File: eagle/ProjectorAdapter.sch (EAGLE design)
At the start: 8 parts, among them J1 0532610271, J3 0532610471, J4 0532610271

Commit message: updated pcb with molex connectors; created 6 pin connector. updated code for different pin definitions.
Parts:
- removed J4: 0532610271, volks73-Molex:0532610271
- added J2: 05339805711, volks73-Molex:05339805711
- J1: value 0532610271 -> 05339805711; device volks73-Molex:0532610271 -> volks73-Molex:05339805711
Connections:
- net FROM_PROJ: now also J2-2.P$1; no longer J4-1.P$1
- net GND: now also J1-3.P$1, J2-3.P$1; no longer J1-1.P$1, J4-2.P$1
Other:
- moved on the sheet: J1-1, J1-2
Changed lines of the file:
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@@
 <part name="GND3" library="SparkFun-Aesthetics" deviceset="GND" device=""/>
 <part name="J3" library="volks73-Molex" deviceset="0532610471" device=""/>
-<part name="J1" library="volks73-Molex" deviceset="0532610271" device=""/>
-<part name="J4" library="volks73-Molex" deviceset="0532610271" device=""/>
+<part name="J1" library="volks73-Molex" deviceset="05339805711" device=""/>
+<part name="J2" library="volks73-Molex" deviceset="05339805711" device=""/>
 <part name="GND1" library="SparkFun-Aesthetics" deviceset="GND" device=""/>
 <part name="GND4" library="SparkFun-Aesthetics" deviceset="GND" device=""/>
@@
 <instance part="J3" gate="-3" x="93.98" y="-27.94"/>
 <instance part="J3" gate="-4" x="93.98" y="-38.1"/>
-<instance part="J1" gate="-1" x="127" y="25.4"/>
-<instance part="J1" gate="-2" x="127" y="30.48"/>
-<instance part="J4" gate="-1" x="-15.24" y="33.02" rot="R180"/>
-<instance part="J4" gate="-2" x="-15.24" y="25.4" rot="R180"/>
-<instance part="GND1" gate="1" x="-7.62" y="7.62"/>
-<instance part="GND4" gate="1" x="114.3" y="5.08"/>
+<instance part="J1" gate="-1" x="139.7" y="40.64"/>
+<instance part="J1" gate="-2" x="139.7" y="27.94"/>
+<instance part="J1" gate="-3" x="139.7" y="17.78"/>
+<instance part="J1" gate="-4" x="139.7" y="7.62"/>
+<instance part="J1" gate="-5" x="142.24" y="-7.62"/>
+<instance part="J1" gate="-6" x="139.7" y="-20.32"/>
+<instance part="J2" gate="-1" x="-30.48" y="58.42" rot="R180"/>
+<instance part="J2" gate="-2" x="-30.48" y="45.72" rot="R180"/>
+<instance part="J2" gate="-3" x="-30.48" y="33.02" rot="R180"/>
+<instance part="J2" gate="-4" x="-30.48" y="25.4" rot="R180"/>
+<instance part="J2" gate="-5" x="-30.48" y="15.24" rot="R180"/>
+<instance part="J2" gate="-6" x="-30.48" y="-5.08" rot="R180"/>
+<instance part="GND1" gate="1" x="0" y="20.32"/>
+<instance part="GND4" gate="1" x="111.76" y="10.16"/>
 </instances>
 <busses>
@@
 </segment>
 <segment>
-<pinref part="J4" gate="-2" pin="P$1"/>
-<wire x1="-10.16" y1="25.4" x2="-7.62" y2="25.4" width="0.1524" layer="91"/>
-<wire x1="-7.62" y1="25.4" x2="-7.62" y2="10.16" width="0.1524" layer="91"/>
+<pinref part="J2" gate="-3" pin="P$1"/>
+<wire x1="-25.4" y1="33.02" x2="-2.54" y2="33.02" width="0.1524" layer="91"/>
 <pinref part="GND1" gate="1" pin="GND"/>
+<wire x1="-2.54" y1="33.02" x2="0" y2="33.02" width="0.1524" layer="91"/>
+<wire x1="0" y1="33.02" x2="0" y2="22.86" width="0.1524" layer="91"/>
 </segment>
 <segment>
-<wire x1="114.3" y1="25.4" x2="114.3" y2="7.62" width="0.1524" layer="91"/>
+<pinref part="J1" gate="-3" pin="P$1"/>
+<wire x1="134.62" y1="17.78" x2="111.76" y2="17.78" width="0.1524" layer="91"/>
+<wire x1="111.76" y1="17.78" x2="111.76" y2="12.7" width="0.1524" layer="91"/>
 <pinref part="GND4" gate="1" pin="GND"/>
-<pinref part="J1" gate="-1" pin="P$1"/>
-<wire x1="121.92" y1="25.4" x2="114.3" y2="25.4" width="0.1524" layer="91"/>
 </segment>
 </net>
@@
 <net name="FROM_PROJ" class="0">
 <segment>
-<pinref part="J4" gate="-1" pin="P$1"/>
-<wire x1="-10.16" y1="33.02" x2="-2.54" y2="33.02" width="0.1524" layer="91"/>
-<label x="0" y="33.02" size="1.778" layer="95"/>
-</segment>
-<segment>
 <pinref part="TEENSY_LEFT" gate="G$1" pin="4"/>
 <wire x1="40.64" y1="45.72" x2="30.48" y2="45.72" width="0.1524" layer="91"/>
 <label x="22.86" y="45.72" size="1.778" layer="95"/>
+</segment>
+<segment>
+<pinref part="J2" gate="-2" pin="P$1"/>
+<wire x1="-25.4" y1="45.72" x2="0" y2="45.72" width="0.1524" layer="91"/>
+<label x="-5.08" y="48.26" size="1.778" layer="95"/>
 </segment>
 </net>
@@
 </segment>
 </net>
-<net name="N$1" class="0">
+<net name="N$4" class="0">
 <segment>
+<pinref part="J1" gate="-2" pin="P$1"/>
+<wire x1="121.92" y1="27.94" x2="134.62" y2="27.94" width="0.1524" layer="91"/>
 <pinref part="R1" gate="G$1" pin="2"/>
-<pinref part="J1" gate="-2" pin="P$1"/>
 <wire x1="114.3" y1="30.48" x2="121.92" y2="30.48" width="0.1524" layer="91"/>
+<wire x1="121.92" y1="27.94" x2="121.92" y2="30.48" width="0.1524" layer="91"/>
 </segment>
 </net>

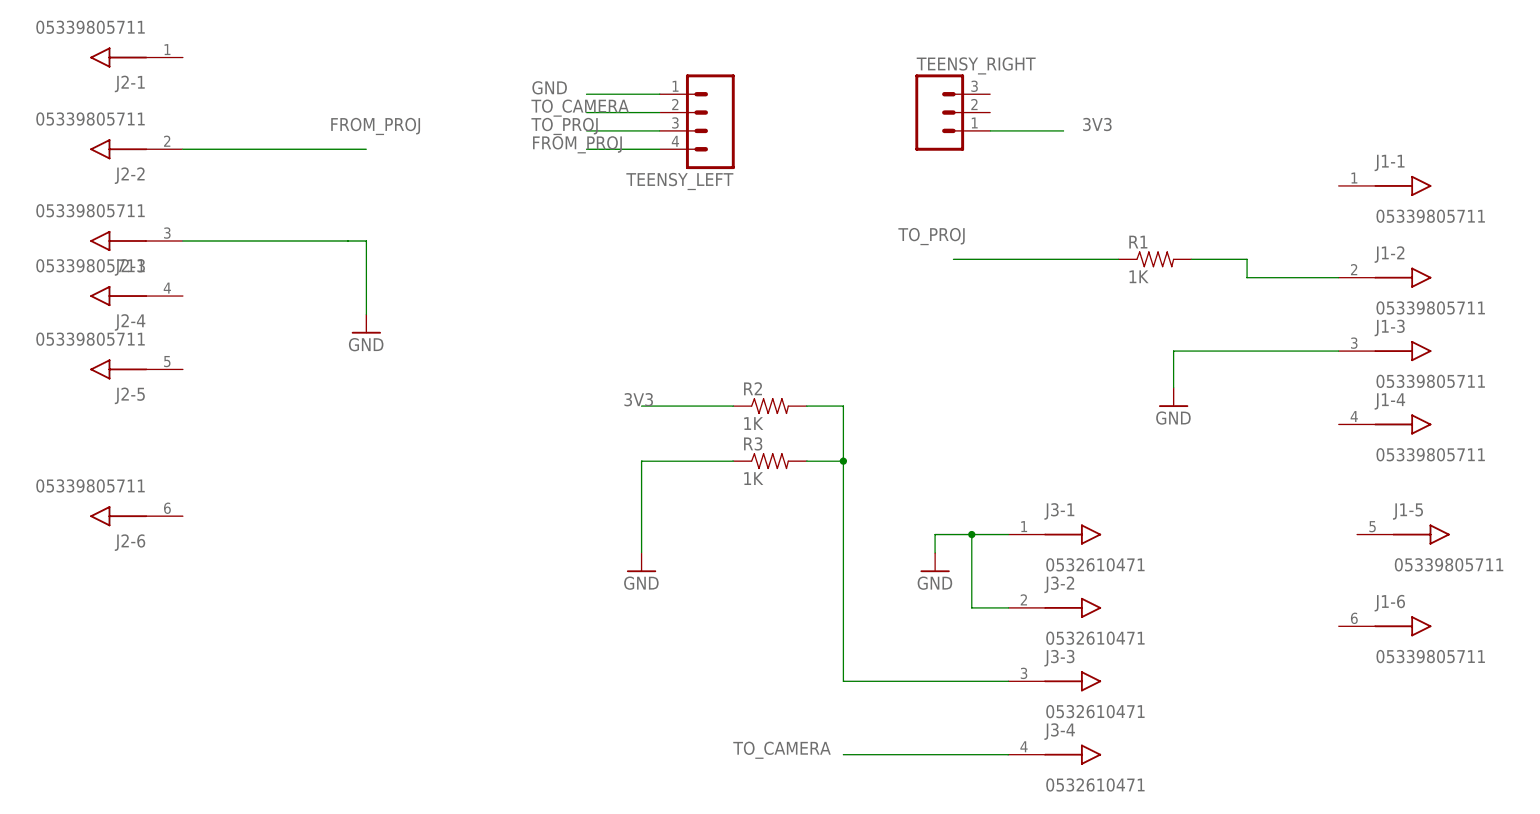
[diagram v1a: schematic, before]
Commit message: designed rev3 board to cover full teensy bottom and mount below it.
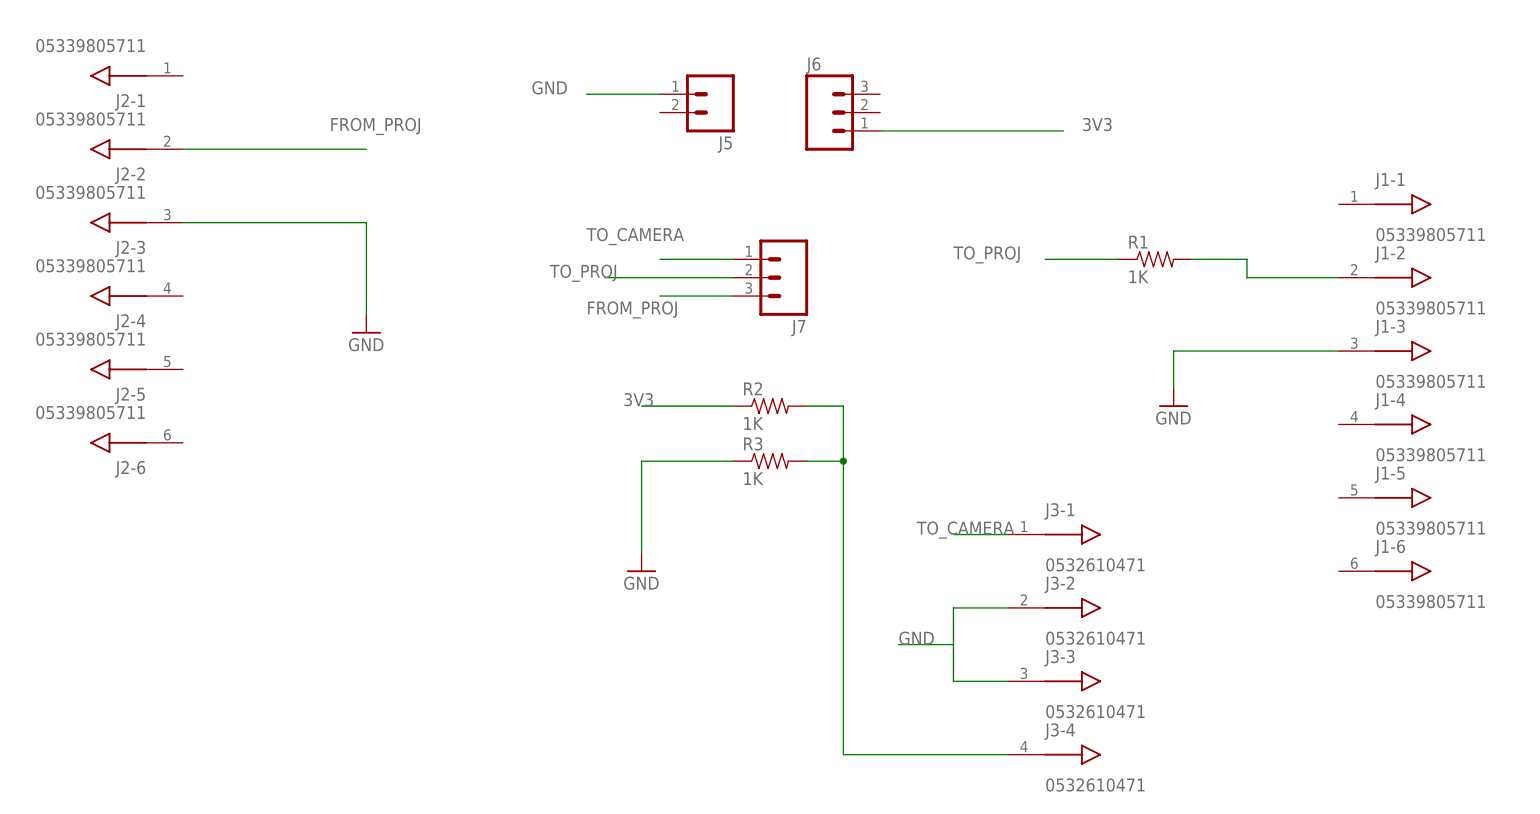
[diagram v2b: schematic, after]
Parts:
- removed TEENSY_LEFT: (no value), SparkFun-Connectors:M04PTH
- removed TEENSY_RIGHT: (no value), SparkFun-Connectors:M03PTH
- added J5: (no value), SparkFun-Connectors:M02PTH
- added J6, J7: (no value), SparkFun-Connectors:M03PTH
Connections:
- net 3V3: now also J6.1; no longer TEENSY_RIGHT.1
- net FROM_PROJ: now also J7.3; no longer TEENSY_LEFT.4
- net GND: now also J3-3.P$1, J5.1; no longer J3-1.P$1, TEENSY_LEFT.1
- net N$2: now also J3-4.P$1; no longer J3-3.P$1
- net TO_CAMERA: now also J3-1.P$1, J7.1; no longer J3-4.P$1, TEENSY_LEFT.2
- net TO_PROJ: now also J7.2; no longer TEENSY_LEFT.3
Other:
- moved on the sheet: J1-1, J1-5, J1-6, J2-1, J2-3, J2-6
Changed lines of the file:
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@@
 </classes>
 <parts>
-<part name="TEENSY_LEFT" library="SparkFun-Connectors" deviceset="M04" device="PTH"/>
-<part name="TEENSY_RIGHT" library="SparkFun-Connectors" deviceset="M03" device="PTH"/>
 <part name="R1" library="SparkFun-Passives" deviceset="RESISTOR" device="0603-RES" value="1K"/>
-<part name="GND2" library="SparkFun-Aesthetics" deviceset="GND" device=""/>
 <part name="R2" library="SparkFun-Passives" deviceset="RESISTOR" device="0603-RES" value="1K"/>
 <part name="R3" library="SparkFun-Passives" deviceset="RESISTOR" device="0603-RES" value="1K"/>
@@
 <part name="GND1" library="SparkFun-Aesthetics" deviceset="GND" device=""/>
 <part name="GND4" library="SparkFun-Aesthetics" deviceset="GND" device=""/>
+<part name="J5" library="SparkFun-Connectors" deviceset="M02" device="PTH"/>
+<part name="J6" library="SparkFun-Connectors" deviceset="M03" device="PTH"/>
+<part name="J7" library="SparkFun-Connectors" deviceset="M03" device="PTH"/>
 </parts>
 <sheets>
@@
 </plain>
 <instances>
-<instance part="TEENSY_LEFT" gate="G$1" x="45.72" y="50.8" rot="R180"/>
-<instance part="TEENSY_RIGHT" gate="J$1" x="78.74" y="50.8"/>
 <instance part="R1" gate="G$1" x="109.22" y="30.48"/>
-<instance part="GND2" gate="1" x="78.74" y="-12.7"/>
 <instance part="R2" gate="G$1" x="55.88" y="10.16"/>
 <instance part="R3" gate="G$1" x="55.88" y="2.54"/>
@@
 <instance part="J3" gate="-3" x="93.98" y="-27.94"/>
 <instance part="J3" gate="-4" x="93.98" y="-38.1"/>
-<instance part="J1" gate="-1" x="139.7" y="40.64"/>
+<instance part="J1" gate="-1" x="139.7" y="38.1"/>
 <instance part="J1" gate="-2" x="139.7" y="27.94"/>
 <instance part="J1" gate="-3" x="139.7" y="17.78"/>
 <instance part="J1" gate="-4" x="139.7" y="7.62"/>
-<instance part="J1" gate="-5" x="142.24" y="-7.62"/>
-<instance part="J1" gate="-6" x="139.7" y="-20.32"/>
-<instance part="J2" gate="-1" x="-30.48" y="58.42" rot="R180"/>
+<instance part="J1" gate="-5" x="139.7" y="-2.54"/>
+<instance part="J1" gate="-6" x="139.7" y="-12.7"/>
+<instance part="J2" gate="-1" x="-30.48" y="55.88" rot="R180"/>
 <instance part="J2" gate="-2" x="-30.48" y="45.72" rot="R180"/>
-<instance part="J2" gate="-3" x="-30.48" y="33.02" rot="R180"/>
+<instance part="J2" gate="-3" x="-30.48" y="35.56" rot="R180"/>
 <instance part="J2" gate="-4" x="-30.48" y="25.4" rot="R180"/>
 <instance part="J2" gate="-5" x="-30.48" y="15.24" rot="R180"/>
-<instance part="J2" gate="-6" x="-30.48" y="-5.08" rot="R180"/>
+<instance part="J2" gate="-6" x="-30.48" y="5.08" rot="R180"/>
 <instance part="GND1" gate="1" x="0" y="20.32"/>
 <instance part="GND4" gate="1" x="111.76" y="10.16"/>
+<instance part="J5" gate="G$1" x="48.26" y="53.34" rot="R180"/>
+<instance part="J6" gate="J$1" x="63.5" y="50.8"/>
+<instance part="J7" gate="J$1" x="58.42" y="27.94" rot="R180"/>
 </instances>
 <busses>
@@
 <net name="GND" class="0">
 <segment>
-<pinref part="TEENSY_LEFT" gate="G$1" pin="1"/>
 <wire x1="40.64" y1="53.34" x2="30.48" y2="53.34" width="0.1524" layer="91"/>
 <label x="22.86" y="53.34" size="1.778" layer="95"/>
-</segment>
-<segment>
-<pinref part="GND2" gate="1" pin="GND"/>
-<pinref part="J3" gate="-1" pin="P$1"/>
-<wire x1="78.74" y1="-7.62" x2="78.74" y2="-10.16" width="0.1524" layer="91"/>
-<wire x1="88.9" y1="-7.62" x2="83.82" y2="-7.62" width="0.1524" layer="91"/>
-<pinref part="J3" gate="-2" pin="P$1"/>
-<wire x1="83.82" y1="-7.62" x2="78.74" y2="-7.62" width="0.1524" layer="91"/>
-<wire x1="88.9" y1="-17.78" x2="83.82" y2="-17.78" width="0.1524" layer="91"/>
-<wire x1="83.82" y1="-17.78" x2="83.82" y2="-7.62" width="0.1524" layer="91"/>
-<junction x="83.82" y="-7.62"/>
+<pinref part="J5" gate="G$1" pin="1"/>
 </segment>
 <segment>
@@
 <segment>
 <pinref part="J2" gate="-3" pin="P$1"/>
-<wire x1="-25.4" y1="33.02" x2="-2.54" y2="33.02" width="0.1524" layer="91"/>
+<wire x1="-25.4" y1="35.56" x2="0" y2="35.56" width="0.1524" layer="91"/>
 <pinref part="GND1" gate="1" pin="GND"/>
-<wire x1="-2.54" y1="33.02" x2="0" y2="33.02" width="0.1524" layer="91"/>
-<wire x1="0" y1="33.02" x2="0" y2="22.86" width="0.1524" layer="91"/>
+<wire x1="0" y1="35.56" x2="0" y2="22.86" width="0.1524" layer="91"/>
 </segment>
 <segment>
@@
 <pinref part="GND4" gate="1" pin="GND"/>
 </segment>
-</net>
-<net name="TO_PROJ" class="0">
 <segment>
-<pinref part="R1" gate="G$1" pin="1"/>
-<wire x1="104.14" y1="30.48" x2="81.28" y2="30.48" width="0.1524" layer="91"/>
-<label x="73.66" y="33.02" size="1.778" layer="95"/>
-</segment>
-<segment>
-<pinref part="TEENSY_LEFT" gate="G$1" pin="3"/>
-<wire x1="40.64" y1="48.26" x2="30.48" y2="48.26" width="0.1524" layer="91"/>
-<label x="22.86" y="48.26" size="1.778" layer="95"/>
+<pinref part="J3" gate="-3" pin="P$1"/>
+<wire x1="88.9" y1="-27.94" x2="81.28" y2="-27.94" width="0.1524" layer="91"/>
+<wire x1="81.28" y1="-27.94" x2="81.28" y2="-22.86" width="0.1524" layer="91"/>
+<pinref part="J3" gate="-2" pin="P$1"/>
+<wire x1="81.28" y1="-22.86" x2="81.28" y2="-17.78" width="0.1524" layer="91"/>
+<wire x1="81.28" y1="-17.78" x2="88.9" y2="-17.78" width="0.1524" layer="91"/>
+<wire x1="81.28" y1="-22.86" x2="73.66" y2="-22.86" width="0.1524" layer="91"/>
+<label x="73.66" y="-22.86" size="1.778" layer="95"/>
 </segment>
 </net>
 <net name="FROM_PROJ" class="0">
-<segment>
-<pinref part="TEENSY_LEFT" gate="G$1" pin="4"/>
-<wire x1="40.64" y1="45.72" x2="30.48" y2="45.72" width="0.1524" layer="91"/>
-<label x="22.86" y="45.72" size="1.778" layer="95"/>
-</segment>
 <segment>
 <pinref part="J2" gate="-2" pin="P$1"/>
@@
 <label x="-5.08" y="48.26" size="1.778" layer="95"/>
 </segment>
+<segment>
+<pinref part="J7" gate="J$1" pin="3"/>
+<wire x1="50.8" y1="25.4" x2="40.64" y2="25.4" width="0.1524" layer="91"/>
+<label x="30.48" y="22.86" size="1.778" layer="95"/>
+</segment>
 </net>
 <net name="TO_CAMERA" class="0">
 <segment>
-<pinref part="J3" gate="-4" pin="P$1"/>
-<wire x1="88.9" y1="-38.1" x2="66.04" y2="-38.1" width="0.1524" layer="91"/>
-<label x="50.8" y="-38.1" size="1.778" layer="95"/>
+<pinref part="J7" gate="J$1" pin="1"/>
+<wire x1="50.8" y1="30.48" x2="40.64" y2="30.48" width="0.1524" layer="91"/>
+<label x="30.48" y="33.02" size="1.778" layer="95"/>
 </segment>
 <segment>
-<pinref part="TEENSY_LEFT" gate="G$1" pin="2"/>
-<wire x1="40.64" y1="50.8" x2="30.48" y2="50.8" width="0.1524" layer="91"/>
-<label x="22.86" y="50.8" size="1.778" layer="95"/>
+<pinref part="J3" gate="-1" pin="P$1"/>
+<wire x1="88.9" y1="-7.62" x2="81.28" y2="-7.62" width="0.1524" layer="91"/>
+<label x="76.2" y="-7.62" size="1.778" layer="95"/>
 </segment>
 </net>
 <net name="3V3" class="0">
 <segment>
-<pinref part="TEENSY_RIGHT" gate="J$1" pin="1"/>
-<wire x1="86.36" y1="48.26" x2="96.52" y2="48.26" width="0.1524" layer="91"/>
 <label x="99.06" y="48.26" size="1.778" layer="95"/>
+<wire x1="96.52" y1="48.26" x2="71.12" y2="48.26" width="0.1524" layer="91"/>
+<pinref part="J6" gate="J$1" pin="1"/>
 </segment>
 <segment>
@@
 <wire x1="60.96" y1="2.54" x2="66.04" y2="2.54" width="0.1524" layer="91"/>
 <wire x1="66.04" y1="2.54" x2="66.04" y2="10.16" width="0.1524" layer="91"/>
-<pinref part="J3" gate="-3" pin="P$1"/>
-<wire x1="88.9" y1="-27.94" x2="66.04" y2="-27.94" width="0.1524" layer="91"/>
-<wire x1="66.04" y1="-27.94" x2="66.04" y2="2.54" width="0.1524" layer="91"/>
+<wire x1="66.04" y1="-38.1" x2="66.04" y2="2.54" width="0.1524" layer="91"/>
 <junction x="66.04" y="2.54"/>
+<pinref part="J3" gate="-4" pin="P$1"/>
+<wire x1="66.04" y1="-38.1" x2="88.9" y2="-38.1" width="0.1524" layer="91"/>
 </segment>
 </net>
@@
 </segment>
 </net>
+<net name="TO_PROJ" class="0">
+<segment>
+<pinref part="J7" gate="J$1" pin="2"/>
+<wire x1="50.8" y1="27.94" x2="33.02" y2="27.94" width="0.1524" layer="91"/>
+<label x="25.4" y="27.94" size="1.778" layer="95"/>
+</segment>
+<segment>
+<pinref part="R1" gate="G$1" pin="1"/>
+<wire x1="104.14" y1="30.48" x2="93.98" y2="30.48" width="0.1524" layer="91"/>
+<label x="81.28" y="30.48" size="1.778" layer="95"/>
+</segment>
+</net>
